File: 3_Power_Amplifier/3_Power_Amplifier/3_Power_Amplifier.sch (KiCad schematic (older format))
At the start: 15 parts, among them P1 IN_FUENTE_CONM, P2 OUT_CON_CAP, P3 OUT_SIN_CAP, P4 CONN_01X02, Q1 IRF740N, Q2 IRF740N, Q3 IRF740N, Q4 IRF740N, T1 TRANSFO-SO12

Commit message: EDICION DE HUELLAS
DEL TRAFO
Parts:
- Q1, Q2, Q3, Q4: footprint TO-220 -> (none)
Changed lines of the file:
@@
 F 0 "Q3" H 4800 1375 50  0001 L CNN
 F 1 "IRF740N" H 4800 1300 50  0000 L CNN
-F 2 "TO-220" H 4800 1225 50  0001 L CIN
+F 2 "" H 4800 1225 50  0001 L CIN
 F 3 "" H 4800 1375 50  0001 L CNN
 F 4 "2400" H 4900 1475 60  0001 C CNN "Didacticas_Electronica"
@@
 F 0 "Q1" H 3350 1375 50  0001 L CNN
 F 1 "IRF740N" H 3350 1300 50  0000 L CNN
-F 2 "TO-220" H 3350 1225 50  0001 L CIN
+F 2 "" H 3350 1225 50  0001 L CIN
 F 3 "" H 3350 1375 50  0001 L CNN
 F 4 "2400" H 3450 1475 60  0001 C CNN "Didacticas_Electronica"
@@
 F 0 "Q4" H 4800 2325 50  0001 L CNN
 F 1 "IRF740N" H 4800 2250 50  0000 L CNN
-F 2 "TO-220" H 4800 2175 50  0001 L CIN
+F 2 "" H 4800 2175 50  0001 L CIN
 F 3 "" H 4800 2325 50  0001 L CNN
 F 4 "2400" H 4900 2425 60  0001 C CNN "Didacticas_Electronica"
@@
 F 0 "Q2" H 3350 2325 50  0001 L CNN
 F 1 "IRF740N" H 3350 2250 50  0000 L CNN
-F 2 "TO-220" H 3350 2175 50  0001 L CIN
+F 2 "" H 3350 2175 50  0001 L CIN
 F 3 "" H 3350 2325 50  0001 L CNN
 F 4 "2400" H 3450 2425 60  0001 C CNN "Didacticas_Electronica"
@@
 F 0 "T1" H 9800 1900 50  0000 C CNN
 F 1 "TRANSFO-SO12" H 9750 1300 50  0000 C CNN
-F 2 "" H 9800 1650 50  0000 C CNN
+F 2 "" H 9800 1650 50  0001 C CNN
 F 3 "" H 9800 1650 50  0000 C CNN
 	1    9800 1650
@@
 F 0 "C1" H 6225 1500 50  0000 L CNN
 F 1 "32nF" H 6225 1300 50  0000 L CNN
-F 2 "" H 6238 1250 50  0000 C CNN
+F 2 "" H 6238 1250 50  0001 C CNN
 F 3 "" H 6225 1500 50  0000 C CNN
 F 4 "para 300kHz" H 6325 1600 60  0001 C CNN "frecuencias"
@@
 F 0 "C3" H 6975 1500 50  0000 L CNN
 F 1 "32nF" H 6975 1300 50  0000 L CNN
-F 2 "" H 6988 1250 50  0000 C CNN
+F 2 "" H 6988 1250 50  0001 C CNN
 F 3 "" H 6975 1500 50  0000 C CNN
 F 4 "para 300kHz" H 7075 1600 60  0001 C CNN "frecuencias"
@@
 F 0 "C2" H 6225 2050 50  0000 L CNN
 F 1 "32nF" H 6225 1850 50  0000 L CNN
-F 2 "" H 6238 1800 50  0000 C CNN
+F 2 "" H 6238 1800 50  0001 C CNN
 F 3 "" H 6225 2050 50  0000 C CNN
 F 4 "para 300kHz" H 6325 2150 60  0001 C CNN "frecuencias"
@@
 F 0 "C4" H 6975 2050 50  0000 L CNN
 F 1 "32nF" H 6975 1850 50  0000 L CNN
-F 2 "" H 6988 1800 50  0000 C CNN
+F 2 "" H 6988 1800 50  0001 C CNN
 F 3 "" H 6975 2050 50  0000 C CNN
 F 4 "para 300kHz" H 7075 2150 60  0001 C CNN "frecuencias"
@@
 F 0 "P1" H 950 1500 50  0000 C CNN
 F 1 "IN_FUENTE_CONM" V 1050 1350 50  0000 C CNN
-F 2 "" H 950 1350 50  0000 C CNN
+F 2 "" H 950 1350 50  0001 C CNN
 F 3 "" H 950 1350 50  0000 C CNN
 	1    950  1350
@@
 F 0 "P2" H 950 2250 50  0000 C CNN
 F 1 "OUT_CON_CAP" V 1050 2100 50  0000 C CNN
-F 2 "" H 950 2100 50  0000 C CNN
+F 2 "" H 950 2100 50  0001 C CNN
 F 3 "" H 950 2100 50  0000 C CNN
 	1    950  2100
@@
 F 0 "P3" H 950 2950 50  0000 C CNN
 F 1 "OUT_SIN_CAP" V 1050 2800 50  0000 C CNN
-F 2 "" H 950 2800 50  0000 C CNN
+F 2 "" H 950 2800 50  0001 C CNN
 F 3 "" H 950 2800 50  0000 C CNN
 	1    950  2800
@@
 F 0 "C5" H 9625 3750 50  0000 L CNN
 F 1 "32nF" H 9625 3550 50  0000 L CNN
-F 2 "" H 9638 3500 50  0000 C CNN
+F 2 "" H 9638 3500 50  0001 C CNN
 F 3 "" H 9600 3650 50  0000 C CNN
 	1    9600 3650
@@
 F 0 "C6" H 9625 4250 50  0000 L CNN
 F 1 "32nF" H 9625 4050 50  0000 L CNN
-F 2 "" H 9638 4000 50  0000 C CNN
+F 2 "" H 9638 4000 50  0001 C CNN
 F 3 "" H 9600 4150 50  0000 C CNN
 	1    9600 4150
@@
 F 0 "P4" H 950 3500 50  0000 C CNN
 F 1 "CONN_01X02" V 1050 3350 50  0000 C CNN
-F 2 "" H 950 3350 50  0000 C CNN
+F 2 "" H 950 3350 50  0001 C CNN
 F 3 "" H 950 3350 50  0000 C CNN
 	1    950  3350

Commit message: DISEÑO_PCB
PRIMER DISEÑO DE PCB
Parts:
- removed C5, C6: 32nF, symbol C
- added C5, C6: 32nF, Capacitors_THT:C_Disc_D8.0mm_W2.5mm_P5.00mm, symbol 32nF
- C1, C2, C3, C4: footprint (none) -> Capacitors_THT:C_Disc_D8.0mm_W2.5mm_P5.00mm
- P1, P2, P3: footprint (none) -> Sockets_MOLEX_KK-System:Socket_MOLEX-KK-RM3-96mm_Lock_2pin_straight
- P4: footprint (none) -> Pin_Headers:Pin_Header_Angled_1x02_Pitch2.54mm
- Q1, Q2, Q3, Q4: footprint (none) -> TO_SOT_Packages_THT:TO-220_Vertical
- T1: footprint (none) -> libreria_Power_Amplifier_huellas:foot_print_trafo

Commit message: AMPLIFICADOR DE POTENCIA_2 PCBS
el transformador con array capacitivo y mosfet con disipadores
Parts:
- removed C1, C2, C3, C4, C5, C6: 32nF, Capacitors_THT:C_Disc_D8.0mm_W2.5mm_P5.00mm, symbol 32nF
- removed P1: IN_FUENTE_CONM, Sockets_MOLEX_KK-System:Socket_MOLEX-KK-RM3-96mm_Lock_2pin_straight, symbol IN_FUENTE_CONM
- removed P2: OUT_CON_CAP, Sockets_MOLEX_KK-System:Socket_MOLEX-KK-RM3-96mm_Lock_2pin_straight, symbol OUT_CON_CAP
- removed P3: OUT_SIN_CAP, Sockets_MOLEX_KK-System:Socket_MOLEX-KK-RM3-96mm_Lock_2pin_straight, symbol OUT_SIN_CAP
- removed P4: CONN_01X02, Pin_Headers:Pin_Header_Angled_1x02_Pitch2.54mm, symbol CONN_01X02
- removed T1: TRANSFO-SO12, libreria_Power_Amplifier_huellas:foot_print_trafo, symbol TRANSFO-SO12
- added P1: INPUT_SIGNAL, Pin_Headers:Pin_Header_Angled_1x02_Pitch2.54mm, symbol INPUT_SIGNAL
- added P2: OUT_SWITCHEO, Sockets_MOLEX_KK-System:Socket_MOLEX-KK-RM3-96mm_Lock_4pin_straight, symbol OUT_SWITCHEO
- added R1, R3, R5, R7: 100, Resistors_THT:R_Axial_DIN0207_L6.3mm_D2.5mm_P7.62mm_Horizontal, symbol 100
- added R2, R4, R6, R8: 10K, Resistors_THT:R_Axial_DIN0207_L6.3mm_D2.5mm_P7.62mm_Horizontal, symbol 10K
- Q1, Q2, Q3, Q4: footprint TO_SOT_Packages_THT:TO-220_Vertical -> libreria_Power_Amplifier_huellas:TO-220_Vertical
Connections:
- net labels added: DDS, SWITCHEO
- net labels removed: ARRAY_CAP, INPUT_SIGNAL, OUT_POT_ONE, OUT_POT_TWO, OUT_SISTEM_ONE, OUT_SISTEM_TWO, SIGNAL_PWM
- wire segments 39 -> 30
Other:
- note added: "CONECTORES\nENTRADA\n"
- note added: "POWER AMPLIFIER PART 1"
- note removed: "ARREGLO DE CAPACITORES"
- note removed: "CAPACITORES EMI\n"
- note removed: "CONECTORES\n"
- note removed: "TRANSFORMADOR AMPLIFICADOR DE POTENCIA"

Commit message: AMPLIFICADOR DE POTENCIA_2 PCB_UNO
CON ISLETAS Y DISIPADORES VERTICALES
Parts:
- removed P2: OUT_SWITCHEO, Sockets_MOLEX_KK-System:Socket_MOLEX-KK-RM3-96mm_Lock_4pin_straight, symbol OUT_SWITCHEO
- removed Q1, Q2, Q3, Q4: IRF740N, libreria_Power_Amplifier_huellas:TO-220_Vertical, symbol IRF740N
- added P2: TIERRA, libreria_Power_Amplifier_huellas:Socket_MOLEX-2-pin-invertido, symbol TIERRA
- added P3, P4, P5, P6: ISLETA, Mounting_Holes:MountingHole_3.2mm_M3_Pad_Via, symbol ISLETA
- added P7: OUT_SWITCHEO, libreria_Power_Amplifier_huellas:Socket_MOLEX-2-pin-invertido, symbol OUT_SWITCHEO
- added P8: TIERRAA, Pin_Headers:Pin_Header_Straight_1x02_Pitch2.54mm, symbol TIERRAA
- added Q1, Q2, Q3, Q4: IRF740NPBF, libreria_Power_Amplifier_huellas:TO-220_Ver_Disipador, symbol IRF740NPBF
- P1: footprint Pin_Headers:Pin_Header_Angled_1x02_Pitch2.54mm -> libreria_Power_Amplifier_huellas:Pin_Header_Pitch2.54mm_NEW
- R1, R2, R3, R4, R5, R6, R7, R8: footprint Resistors_THT:R_Axial_DIN0207_L6.3mm_D2.5mm_P7.62mm_Horizontal -> libreria_Power_Amplifier_huellas:R_Axia_P7.62mm_Horizontal_INV
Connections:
- wire segments 30 -> 32
- no-connect marks 0 -> 8

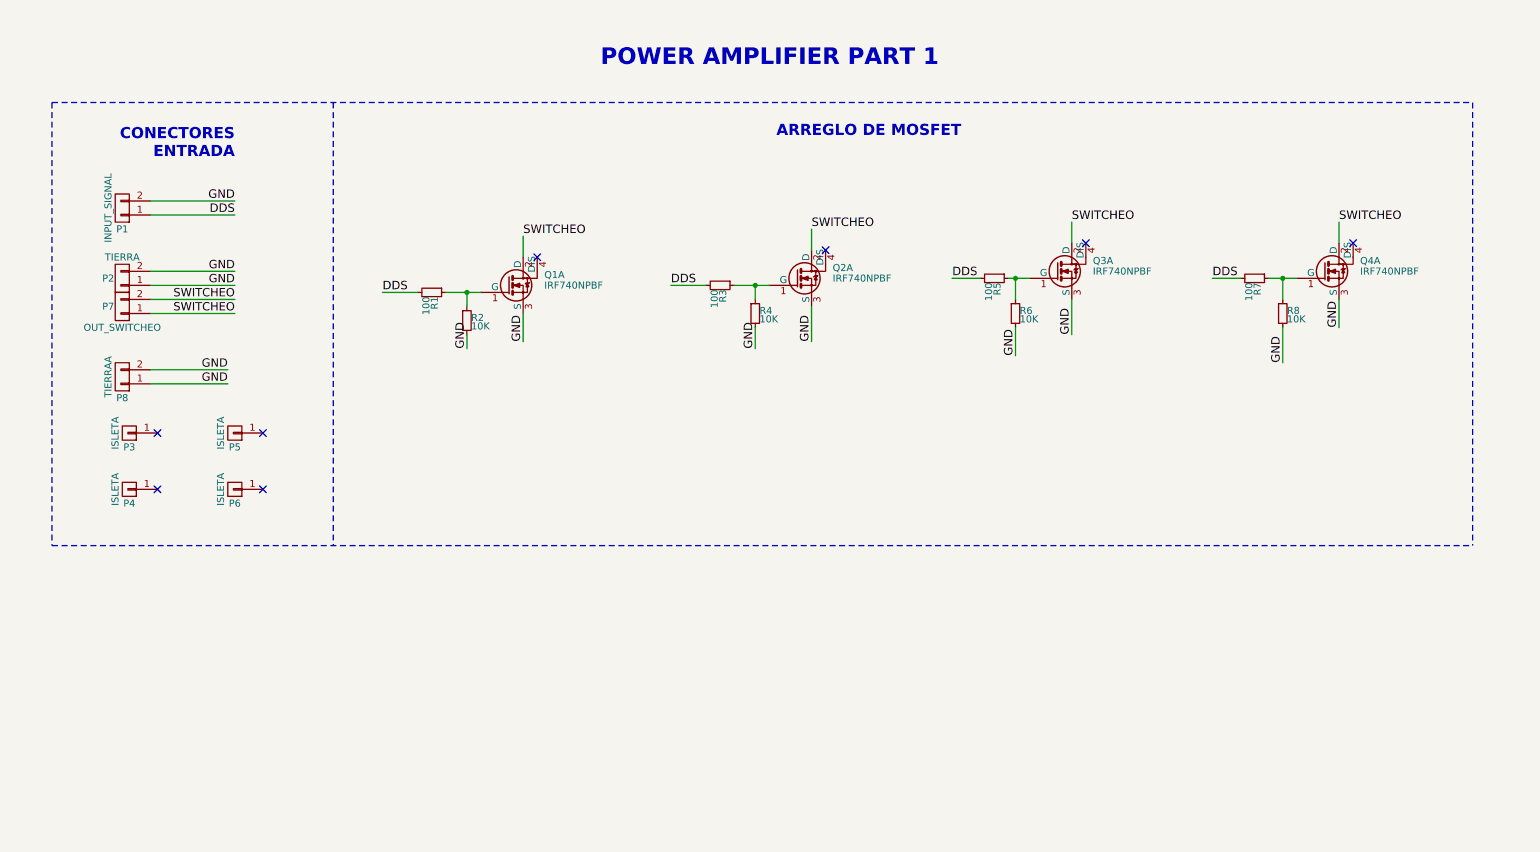
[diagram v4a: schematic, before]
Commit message: AMPLIFICADOR DE POTENCIA_2 PCB_V3
MODIFICACION DE HUELLAS DEL COOLER Y PLANOS A SOLIDOS
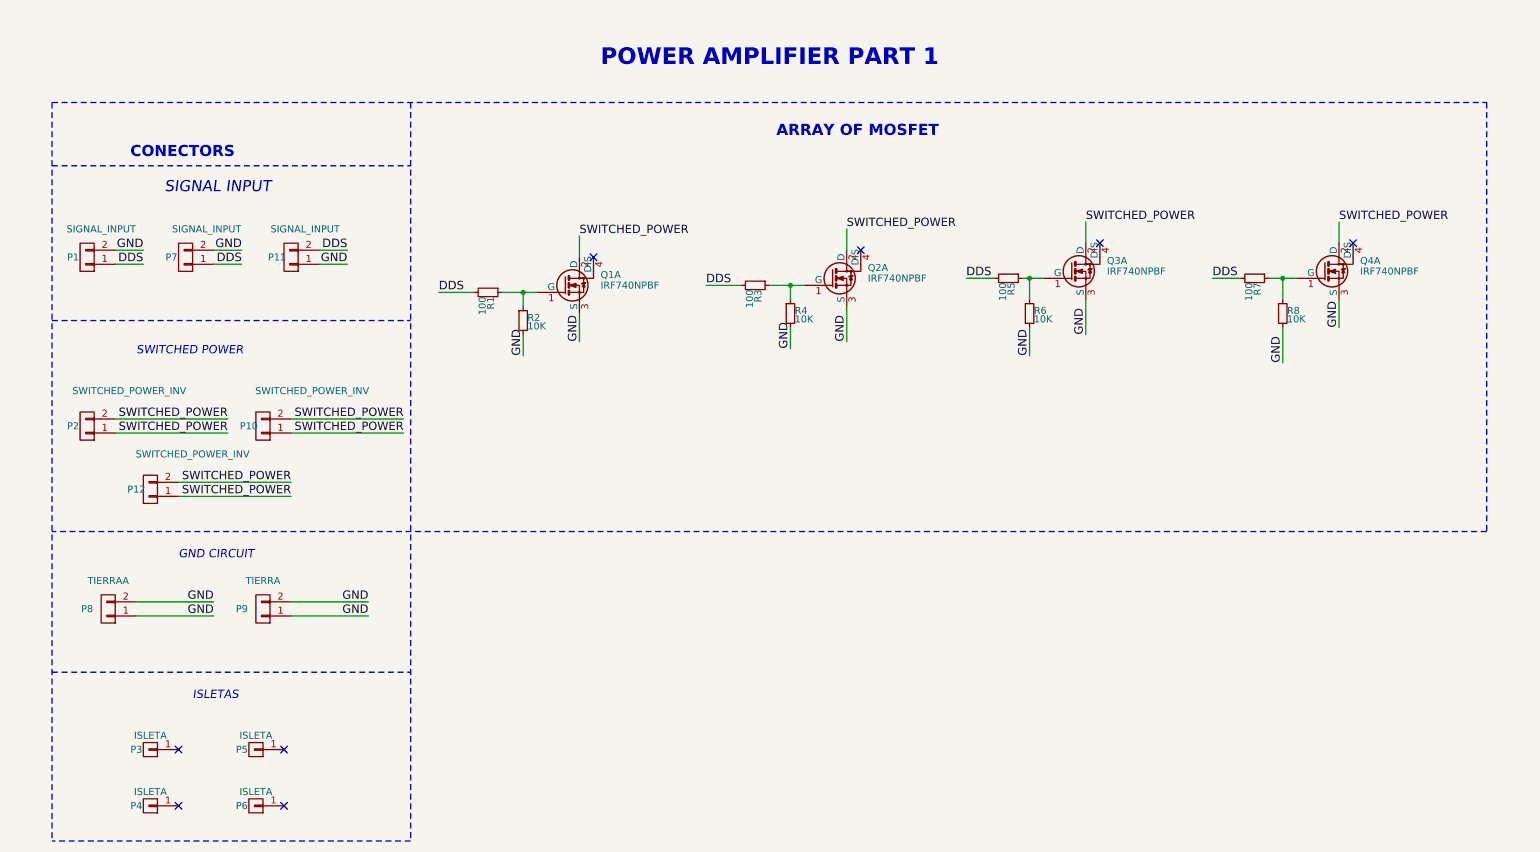
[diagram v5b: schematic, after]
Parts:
- removed P1: INPUT_SIGNAL, libreria_Power_Amplifier_huellas:Pin_Header_Pitch2.54mm_NEW, symbol INPUT_SIGNAL
- removed P2: TIERRA, libreria_Power_Amplifier_huellas:Socket_MOLEX-2-pin-invertido, symbol TIERRA
- removed P7: OUT_SWITCHEO, libreria_Power_Amplifier_huellas:Socket_MOLEX-2-pin-invertido, symbol OUT_SWITCHEO
- added P1, P11, P7: SIGNAL_INPUT, libreria_Power_Amplifier_huellas:REDISEÑADO_INV_Pin_Header_Pitch2.54mm, symbol SIGNAL_INPUT
- added P10, P12, P2: SWITCHED_POWER_INV, libreria_Power_Amplifier_huellas:INV_Socket_MOLEX-2-pines, symbol SWITCHED_POWER_INV
- added P9: TIERRA, libreria_Power_Amplifier_huellas:INV_Socket_MOLEX-2-pines, symbol TIERRA
- R1, R2, R3, R4, R5, R6, R7, R8: footprint libreria_Power_Amplifier_huellas:R_Axia_P7.62mm_Horizontal_INV -> libreria_Power_Amplifier_huellas:INV_R_0805_HandSoldering
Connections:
- net DDS: now also P1.1 (P1), P11.2 (P2), P7.1 (P1)
- net GND: now also P1.2 (P2), P11.1 (P1), P7.2 (P2), P9.1 (P1), P9.2 (P2)
- net SWITCHEO renamed SWITCHED_POWER
- net SWITCHED_POWER: now also P10.1 (P1), P10.2 (P2), P12.1 (P1), P12.2 (P2), P2.1 (P1), P2.2 (P2)
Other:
- note added: "ARRAY OF MOSFET \n"
- note added: "CONECTORS\n"
- note added: "GND CIRCUIT"
- note added: "ISLETAS"
- note added: "SIGNAL INPUT"
- note added: "SWITCHED POWER\n"
- note removed: "ARREGLO DE MOSFET \n"
- note removed: "CONECTORES\nENTRADA\n"
- moved on the sheet: P3, P4, P5, P6, P8, Q1A, Q2A, Q3A

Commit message: GENERADOR_V6
ESQUEMATICO LISTO PERO POR REVISAR
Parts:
- removed P1: SIGNAL_INPUT, libreria_Power_Amplifier_huellas:REDISEÑADO_INV_Pin_Header_Pitch2.54mm, symbol SIGNAL_INPUT
- removed P8: TIERRAA, Pin_Headers:Pin_Header_Straight_1x02_Pitch2.54mm, symbol TIERRAA
- added P1: SIGNAL_INPUT_SMA, libreria_Power_Amplifier_huellas:INV_SMA_THT_Jack_Straight, symbol SIGNAL_INPUT_SMA
- added P8: TIERRA, libreria_Power_Amplifier_huellas:INV_Socket_MOLEX-2-pines, symbol TIERRA
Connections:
- net DDS: now also P1.1 (P1)
- net GND: now also P1.2 (P2), P8.1 (P1), P8.2 (P2)
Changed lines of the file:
@@
 GND
-$Comp
-L TIERRAA P8
-U 1 1 59D06E38
-P 1050 4750
-F 0 "P8" H 1200 4750 50  0000 C CNN
-F 1 "TIERRAA" H 1050 4550 50  0000 C CNN
-F 2 "Pin_Headers:Pin_Header_Straight_1x02_Pitch2.54mm" H 950 4800 50  0001 C CNN
-F 3 "" H 1050 4750 50  0000 C CNN
-	1    1050 4750
-	-1   0    0    1
-$EndComp
 $Comp
 L ISLETA P3
@@
 	-1   0    0    1
 $EndComp
-$Comp
-L SIGNAL_INPUT P1
-U 1 1 59D21F96
-P 900 2250
-F 0 "P1" H 1000 2250 50  0000 C CNN
-F 1 "SIGNAL_INPUT" H 800 2050 50  0000 C CNN
-F 2 "libreria_Power_Amplifier_huellas:REDISEÑADO_INV_Pin_Header_Pitch2.54mm" H 800 2300 50  0001 C CNN
-F 3 "" H 900 2400 50  0000 C CNN
-	1    900  2250
-	-1   0    0    1
-$EndComp
 Wire Wire Line
 	1100 2200 1300 2200
@@
 	1    0    0    -1
 $EndComp
+$Comp
+L SIGNAL_INPUT_SMA P1
+U 1 1 59E3490C
+P 900 2250
+F 0 "P1" H 1000 2260 50  0000 C CNN
+F 1 "SIGNAL_INPUT_SMA" H 790 2040 50  0000 C CNN
+F 2 "libreria_Power_Amplifier_huellas:INV_SMA_THT_Jack_Straight" H 800 2300 50  0001 C CNN
+F 3 "" H 900 2400 50  0000 C CNN
+	1    900  2250
+	-1   0    0    1
+$EndComp
+$Comp
+L TIERRA P8
+U 1 1 59E35104
+P 1050 4750
+F 0 "P8" H 1200 4750 50  0000 C CNN
+F 1 "TIERRA" H 1050 4550 50  0000 C CNN
+F 2 "libreria_Power_Amplifier_huellas:INV_Socket_MOLEX-2-pines" H 950 4800 50  0001 C CNN
+F 3 "" H 1050 4900 50  0000 C CNN
+	1    1050 4750
+	-1   0    0    1
+$EndComp
 $EndSCHEMATC

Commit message: GENERADOR_V8
ORGANIZACION DE ELEMENTOS
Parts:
- R1, R2, R3, R4, R5, R6, R7, R8: footprint libreria_Power_Amplifier_huellas:INV_R_0805_HandSoldering -> Resistors_SMD:R_0805_HandSoldering
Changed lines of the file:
@@
 	3200 6400 650  6400
-$Comp
-L 100 R1
-U 1 1 59D2EF68
-P 3750 2500
-F 0 "R1" H 3780 2520 50  0000 L CNN
-F 1 "100" H 3780 2460 50  0000 L CNN
-F 2 "libreria_Power_Amplifier_huellas:INV_R_0805_HandSoldering" H 3680 2420 50  0001 C CNN
-F 3 "" H 3750 2500 50  0000 C CNN
-	1    3750 2500
-	0    1    1    0
-$EndComp
-$Comp
-L 100 R3
-U 1 1 59D2F0DF
-P 5650 2450
-F 0 "R3" H 5680 2470 50  0000 L CNN
-F 1 "100" H 5680 2410 50  0000 L CNN
-F 2 "libreria_Power_Amplifier_huellas:INV_R_0805_HandSoldering" H 5580 2370 50  0001 C CNN
-F 3 "" H 5650 2450 50  0000 C CNN
-	1    5650 2450
-	0    1    1    0
-$EndComp
-$Comp
-L 100 R5
-U 1 1 59D2F33F
-P 7450 2400
-F 0 "R5" H 7480 2420 50  0000 L CNN
-F 1 "100" H 7480 2360 50  0000 L CNN
-F 2 "libreria_Power_Amplifier_huellas:INV_R_0805_HandSoldering" H 7380 2320 50  0001 C CNN
-F 3 "" H 7450 2400 50  0000 C CNN
-	1    7450 2400
-	0    1    1    0
-$EndComp
-$Comp
-L 100 R7
-U 1 1 59D2F4DC
-P 9200 2400
-F 0 "R7" H 9230 2420 50  0000 L CNN
-F 1 "100" H 9230 2360 50  0000 L CNN
-F 2 "libreria_Power_Amplifier_huellas:INV_R_0805_HandSoldering" H 9130 2320 50  0001 C CNN
-F 3 "" H 9200 2400 50  0000 C CNN
-	1    9200 2400
-	0    1    1    0
-$EndComp
-$Comp
-L 10K R2
-U 1 1 59D2FB7B
-P 4000 2700
-F 0 "R2" H 4030 2720 50  0000 L CNN
-F 1 "10K" H 4030 2660 50  0000 L CNN
-F 2 "libreria_Power_Amplifier_huellas:INV_R_0805_HandSoldering" H 3930 2620 50  0001 C CNN
-F 3 "" H 4000 2700 50  0000 C CNN
-	1    4000 2700
-	1    0    0    -1
-$EndComp
-$Comp
-L 10K R4
-U 1 1 59D2FC1D
-P 5900 2650
-F 0 "R4" H 5930 2670 50  0000 L CNN
-F 1 "10K" H 5930 2610 50  0000 L CNN
-F 2 "libreria_Power_Amplifier_huellas:INV_R_0805_HandSoldering" H 5830 2570 50  0001 C CNN
-F 3 "" H 5900 2650 50  0000 C CNN
-	1    5900 2650
-	1    0    0    -1
-$EndComp
-$Comp
-L 10K R6
-U 1 1 59D2FFBD
-P 7600 2650
-F 0 "R6" H 7630 2670 50  0000 L CNN
-F 1 "10K" H 7630 2610 50  0000 L CNN
-F 2 "libreria_Power_Amplifier_huellas:INV_R_0805_HandSoldering" H 7530 2570 50  0001 C CNN
-F 3 "" H 7600 2650 50  0000 C CNN
-	1    7600 2650
-	1    0    0    -1
-$EndComp
-$Comp
-L 10K R8
-U 1 1 59D301F0
-P 9400 2650
-F 0 "R8" H 9430 2670 50  0000 L CNN
-F 1 "10K" H 9430 2610 50  0000 L CNN
-F 2 "libreria_Power_Amplifier_huellas:INV_R_0805_HandSoldering" H 9330 2570 50  0001 C CNN
-F 3 "" H 9400 2650 50  0000 C CNN
-	1    9400 2650
-	1    0    0    -1
-$EndComp
 $Comp
 L SIGNAL_INPUT_SMA P1
@@
 	-1   0    0    1
 $EndComp
+$Comp
+L 100 R1
+U 1 1 59DA5392
+P 3750 2500
+F 0 "R1" H 3780 2520 50  0000 L CNN
+F 1 "100" H 3780 2460 50  0000 L CNN
+F 2 "Resistors_SMD:R_0805_HandSoldering" H 3680 2420 50  0001 C CNN
+F 3 "" H 3750 2500 50  0000 C CNN
+	1    3750 2500
+	0    1    1    0
+$EndComp
+$Comp
+L 100 R7
+U 1 1 59DA55F1
+P 9200 2400
+F 0 "R7" H 9230 2420 50  0000 L CNN
+F 1 "100" H 9230 2360 50  0000 L CNN
+F 2 "Resistors_SMD:R_0805_HandSoldering" H 9130 2320 50  0001 C CNN
+F 3 "" H 9200 2400 50  0000 C CNN
+	1    9200 2400
+	0    1    1    0
+$EndComp
+$Comp
+L 100 R3
+U 1 1 59DA62D7
+P 5650 2450
+F 0 "R3" H 5680 2470 50  0000 L CNN
+F 1 "100" H 5680 2410 50  0000 L CNN
+F 2 "Resistors_SMD:R_0805_HandSoldering" H 5580 2370 50  0001 C CNN
+F 3 "" H 5650 2450 50  0000 C CNN
+	1    5650 2450
+	0    1    1    0
+$EndComp
+$Comp
+L 100 R5
+U 1 1 59DA63EB
+P 7450 2400
+F 0 "R5" H 7480 2420 50  0000 L CNN
+F 1 "100" H 7480 2360 50  0000 L CNN
+F 2 "Resistors_SMD:R_0805_HandSoldering" H 7380 2320 50  0001 C CNN
+F 3 "" H 7450 2400 50  0000 C CNN
+	1    7450 2400
+	0    1    1    0
+$EndComp
+$Comp
+L 10K R2
+U 1 1 59DA72F3
+P 4000 2700
+F 0 "R2" H 4030 2720 50  0000 L CNN
+F 1 "10K" H 4030 2660 50  0000 L CNN
+F 2 "Resistors_SMD:R_0805_HandSoldering" H 3930 2620 50  0001 C CNN
+F 3 "" H 4000 2700 50  0000 C CNN
+	1    4000 2700
+	1    0    0    -1
+$EndComp
+$Comp
+L 10K R4
+U 1 1 59DA76ED
+P 5900 2650
+F 0 "R4" H 5930 2670 50  0000 L CNN
+F 1 "10K" H 5930 2610 50  0000 L CNN
+F 2 "Resistors_SMD:R_0805_HandSoldering" H 5830 2570 50  0001 C CNN
+F 3 "" H 5900 2650 50  0000 C CNN
+	1    5900 2650
+	1    0    0    -1
+$EndComp
+$Comp
+L 10K R6
+U 1 1 59DA7B59
+P 7600 2650
+F 0 "R6" H 7630 2670 50  0000 L CNN
+F 1 "10K" H 7630 2610 50  0000 L CNN
+F 2 "Resistors_SMD:R_0805_HandSoldering" H 7530 2570 50  0001 C CNN
+F 3 "" H 7600 2650 50  0000 C CNN
+	1    7600 2650
+	1    0    0    -1
+$EndComp
+$Comp
+L 10K R8
+U 1 1 59DA811D
+P 9400 2650
+F 0 "R8" H 9430 2670 50  0000 L CNN
+F 1 "10K" H 9430 2610 50  0000 L CNN
+F 2 "Resistors_SMD:R_0805_HandSoldering" H 9330 2570 50  0001 C CNN
+F 3 "" H 9400 2650 50  0000 C CNN
+	1    9400 2650
+	1    0    0    -1
+$EndComp
 $EndSCHEMATC

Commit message: GENERADOR V_14
ULTIMO DISEÑO CON LOGOS
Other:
- note added: "POWER AMPLIFIER 1"
- note removed: "POWER AMPLIFIER PART 1"
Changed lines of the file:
@@
 	650  1150 650  6400
 Text Notes 4550 900  0    118  ~ 24
-POWER AMPLIFIER PART 1
+POWER AMPLIFIER  1
 Wire Wire Line
 	1100 3400 1900 3400
